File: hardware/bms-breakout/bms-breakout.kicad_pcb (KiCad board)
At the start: 2 copper layers, 116.5 x 125.3 mm, 35 parts, among them J1 IN-A, J10 V-SUPP, J11 Smol_Brain_Board, J13 UART_CONN, J16 ESTOP_CON, J17 I2C_Conn, J18 BAL_3, J19 BAL_2, J2 IN-B, J20 BAL_1, J21 DE9_Socket_MountingHoles, J22 DE9_Socket_MountingHoles, J23 FAN-IN, J24 SWITCH, J3 IN-C, J4 BALANCE-A, J5 BALANCE-B, J6 BALANCE-C, J7 Conn_01x02, Q1 PMOZZ, Q2 NMOS, SW1 Kill_Switch

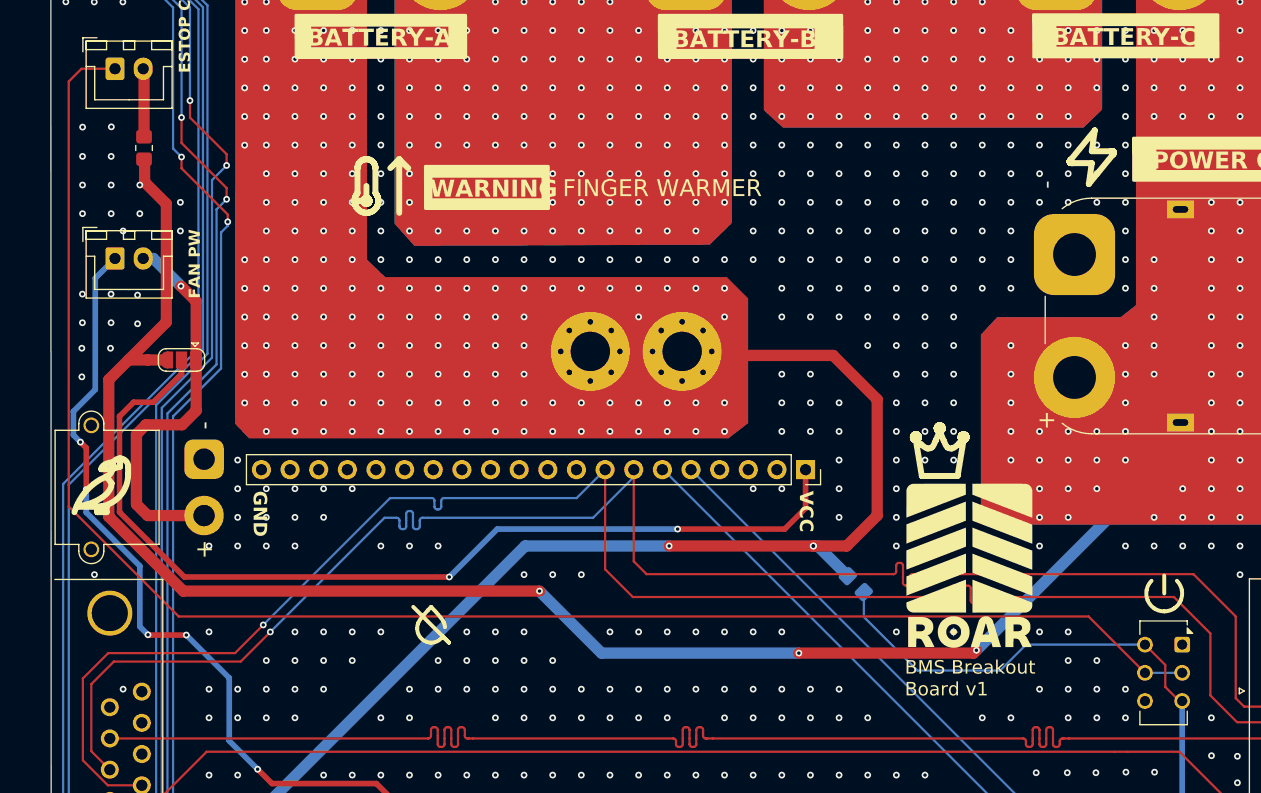
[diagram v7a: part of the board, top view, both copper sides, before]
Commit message: Changed footprint for switch
- Changed footprint for switch
- Edited traces accordingly
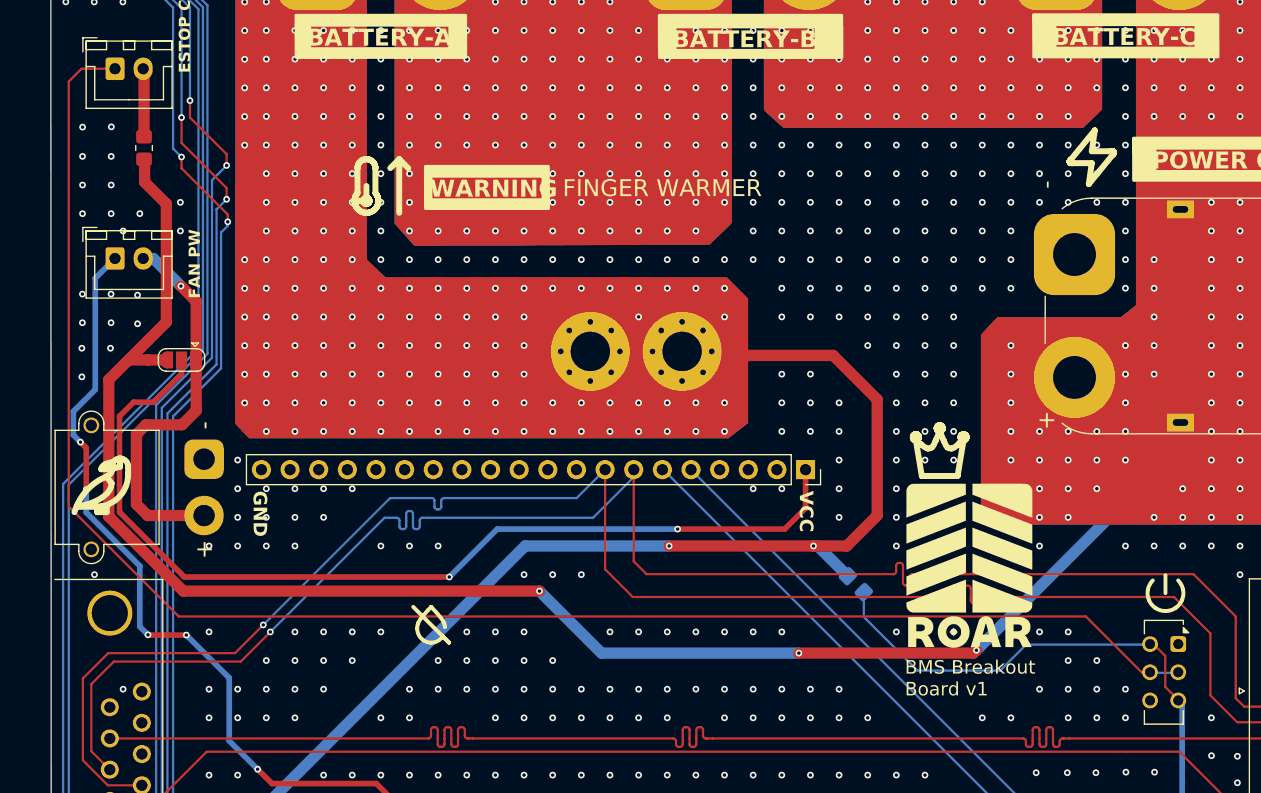
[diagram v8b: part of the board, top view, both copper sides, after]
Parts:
- moved SW1 0.35 mm to (161.5, 114.6)
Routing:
- net Net-(J16-Pin_1): track 147.1 -> 147.8 mm
- net GND_C: vias 604 -> 603
- net GND_B: vias 158 -> 157
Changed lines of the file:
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@@
 	(footprint "Button_Switch_THT:SW_CK_JS202011CQN_DPDT_Straight"
 		(layer "F.Cu")
-		(at 161.85 114.65 -90)
+		(at 161.5 114.6 -90)
 		(descr "C&K sub miniature slide switch, JS series, DPDT, right angle, http://www.ckswitches.com/media/1422/js.pdf")
 		(tags "switch DPDT")
@@
 		(attr through_hole)
 		(fp_line
-			(start -2.1 3.75)
-			(end -0.9 3.75)
+			(start -2.1 3)
+			(end -0.9 3)
 			(stroke
 				(width 0.12)
@@
 		)
 		(fp_line
-			(start 7.1 3.75)
-			(end 5.9 3.75)
+			(start 7.1 3)
+			(end 5.9 3)
 			(stroke
 				(width 0.12)
@@
 		(fp_line
 			(start -2.1 -0.45)
-			(end -2.1 3.75)
+			(end -2.1 3)
 			(stroke
 				(width 0.12)
@@
 		(fp_line
 			(start 7.1 -0.45)
-			(end 7.1 3.75)
+			(end 7.1 3)
 			(stroke
 				(width 0.12)
@@
 		)
 		(fp_line
-			(start -2 3.65)
+			(start -2 3)
 			(end -2 0.65)
 			(stroke
@@
 		)
 		(fp_line
-			(start 7 3.65)
-			(end -2 3.65)
+			(start 7 3)
+			(end -2 3)
 			(stroke
 				(width 0.1)
@@
 		(fp_line
 			(start 7 -0.35)
-			(end 7 3.65)
+			(end 7 3)
 			(stroke
 				(width 0.1)
@@
 		)
 		(pad "4" thru_hole circle
-			(at 5 3.3 270)
+			(at 5 2.5 270)
 			(size 1.4 1.4)
 			(drill 0.9)
@@
 		)
 		(pad "5" thru_hole circle
-			(at 2.5 3.3 270)
+			(at 2.5 2.5 270)
 			(size 1.4 1.4)
 			(drill 0.9)
@@
 		)
 		(pad "6" thru_hole circle
-			(at 0 3.3 270)
+			(at 0 2.5 270)
 			(size 1.4 1.4)
 			(drill 0.9)
@@
 	(gr_curve
 		(pts
-			(xy 161.723636 110.717152) (xy 161.60348 111.007188) (xy 161.399998 111.255103) (xy 161.138943 111.429516)
+			(xy 161.834693 110.687636) (xy 161.714537 110.977672) (xy 161.511055 111.225587) (xy 161.25 111.4)
 		)
 		(stroke
@@
 	(gr_curve
 		(pts
-			(xy 160.257034 111.69701) (xy 159.943079 111.69701) (xy 159.636171 111.60393) (xy 159.375119 111.429516)
+			(xy 160.368091 111.667494) (xy 160.054136 111.667494) (xy 159.747228 111.574414) (xy 159.486176 111.4)
 		)
 		(stroke
@@
 	(gr_curve
 		(pts
-			(xy 159.375119 111.429516) (xy 159.114067 111.255103) (xy 158.910594 111.007188) (xy 158.790424 110.717152)
+			(xy 159.486176 111.4) (xy 159.225124 111.225587) (xy 159.021651 110.977672) (xy 158.901481 110.687636)
 		)
 		(stroke
@@
 	(gr_curve
 		(pts
-			(xy 161.379749 108.987167) (xy 161.601716 109.209204) (xy 161.752864 109.492071) (xy 161.814071 109.8)
+			(xy 161.490806 108.957651) (xy 161.712773 109.179688) (xy 161.863921 109.462555) (xy 161.925128 109.770484)
 		)
 		(stroke
@@
 	)
 	(gr_line
-		(start 160.257722 108.521499)
-		(end 160.257722 110.108999)
+		(start 160.368779 108.491983)
+		(end 160.368779 110.079483)
 		(stroke
 			(width 0.352777)
@@
 	(gr_curve
 		(pts
-			(xy 158.7 109.8) (xy 158.76121 109.492071) (xy 158.912354 109.209204) (xy 159.134318 108.987167)
+			(xy 158.811057 109.770484) (xy 158.872267 109.462555) (xy 159.023411 109.179688) (xy 159.245375 108.957651)
 		)
 		(stroke
@@
 	(gr_curve
 		(pts
-			(xy 161.138943 111.429516) (xy 160.877887 111.60393) (xy 160.570988 111.69701) (xy 160.257034 111.69701)
+			(xy 161.25 111.4) (xy 160.988944 111.574414) (xy 160.682045 111.667494) (xy 160.368091 111.667494)
 		)
 		(stroke
@@
 	(gr_curve
 		(pts
-			(xy 158.790424 110.717152) (xy 158.670255 110.427098) (xy 158.638787 110.10794) (xy 158.7 109.8)
+			(xy 158.901481 110.687636) (xy 158.781312 110.397582) (xy 158.749844 110.078424) (xy 158.811057 109.770484)
 		)
 		(stroke
@@
 	(gr_curve
 		(pts
-			(xy 161.814071 109.8) (xy 161.875278 110.10794) (xy 161.84381 110.427098) (xy 161.723636 110.717152)
+			(xy 161.925128 109.770484) (xy 161.986335 110.078424) (xy 161.954867 110.397582) (xy 161.834693 110.687636)
 		)
 		(stroke
@@
 	)
 	(via
-		(at 129.15 105.9)
-		(size 0.6)
-		(drill 0.3)
-		(layers "F.Cu" "B.Cu")
-		(net 7)
-	)
-	(via
 		(at 83.16 60.18)
 		(size 0.6)
@@
 	)
 	(via
+		(at 129.15 105.9)
+		(size 0.6)
+		(drill 0.3)
+		(layers "F.Cu" "B.Cu")
+		(net 7)
+	)
+	(via
 		(at 83.16 90.66)
 		(size 0.6)
@@
 	)
 	(via
-		(at 129.125 105.9)
-		(size 0.6)
-		(drill 0.3)
-		(layers "F.Cu" "B.Cu")
-		(net 7)
-	)
-	(via
 		(at 78.7 85.59)
 		(size 0.6)
@@
 	)
 	(via
-		(at 69.4 73.885)
-		(size 0.6)
-		(drill 0.3)
-		(layers "F.Cu" "B.Cu")
-		(free yes)
-		(net 8)
-	)
-	(via
 		(at 123.8 72.88)
 		(size 0.6)
@@
 	)
 	(segment
-		(start 158.55 117.15)
-		(end 153.55 112.15)
+		(start 158.3 117.15)
+		(end 158.95 117.15)
 		(width 0.2)
 		(layer "F.Cu")
@@
 	)
 	(segment
-		(start 63.1 102.4)
-		(end 63.1 64.7)
+		(start 67.2 63.575)
+		(end 64.225 63.575)
 		(width 0.2)
 		(layer "F.Cu")
@@
 	(segment
 		(start 72.85 112.15)
-		(end 63.1 102.4)
+		(end 153.3 112.15)
 		(width 0.2)
 		(layer "F.Cu")
@@
 	)
 	(segment
-		(start 63.1 64.7)
-		(end 64.225 63.575)
+		(start 63.1 102.4)
+		(end 72.85 112.15)
 		(width 0.2)
 		(layer "F.Cu")
@@
 	)
 	(segment
-		(start 153.55 112.15)
-		(end 72.85 112.15)
+		(start 158.3 117.15)
+		(end 159.35 117.15)
 		(width 0.2)
 		(layer "F.Cu")
@@
 	(segment
 		(start 64.225 63.575)
-		(end 67.2 63.575)
+		(end 63.1 64.7)
+		(width 0.2)
+		(layer "F.Cu")
+		(net 47)
+	)
+	(segment
+		(start 158.95 117.15)
+		(end 159 117.1)
+		(width 0.2)
+		(layer "F.Cu")
+		(net 47)
+	)
+	(segment
+		(start 153.3 112.15)
+		(end 158.3 117.15)
+		(width 0.2)
+		(layer "F.Cu")
+		(net 47)
+	)
+	(segment
+		(start 63.1 64.7)
+		(end 63.1 102.4)
 		(width 0.2)
 		(layer "F.Cu")
@@
 	)
 	(segment
-		(start 161.85 117.15)
-		(end 158.55 117.15)
+		(start 159.35 117.15)
+		(end 161.85 117.15)
 		(width 0.2)
 		(layer "B.Cu")
@@
 	)
 	(segment
-		(start 160.35 116.45)
-		(end 160.35 118.4)
-		(width 0.2)
-		(layer "F.Cu")
-		(net 62)
-	)
-	(segment
 		(start 163.4125 135.6125)
 		(end 163.05 135.25)
@@
 	(segment
 		(start 158.55 114.65)
-		(end 160.35 116.45)
+		(end 159.35 114.65)
+		(width 0.2)
+		(layer "F.Cu")
+		(net 62)
+	)
+	(segment
+		(start 159.35 114.65)
+		(end 160.35 115.65)
+		(width 0.2)
+		(layer "F.Cu")
+		(net 62)
+	)
+	(segment
+		(start 160.35 115.65)
+		(end 160.35 118.4)
 		(width 0.2)
 		(layer "F.Cu")
